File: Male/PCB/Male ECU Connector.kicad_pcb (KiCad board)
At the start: 2 copper layers, 135 x 41.5 mm, 34 parts, among them J1 ANALYZER, J2 ECU, J3 DJetECUEdgeConnector, U1 TLV76150DCYR, U2 DG333ADW-T1-E3, U3 DG333ADW-T1-E3, U4 DG419BDQ-T1-E3

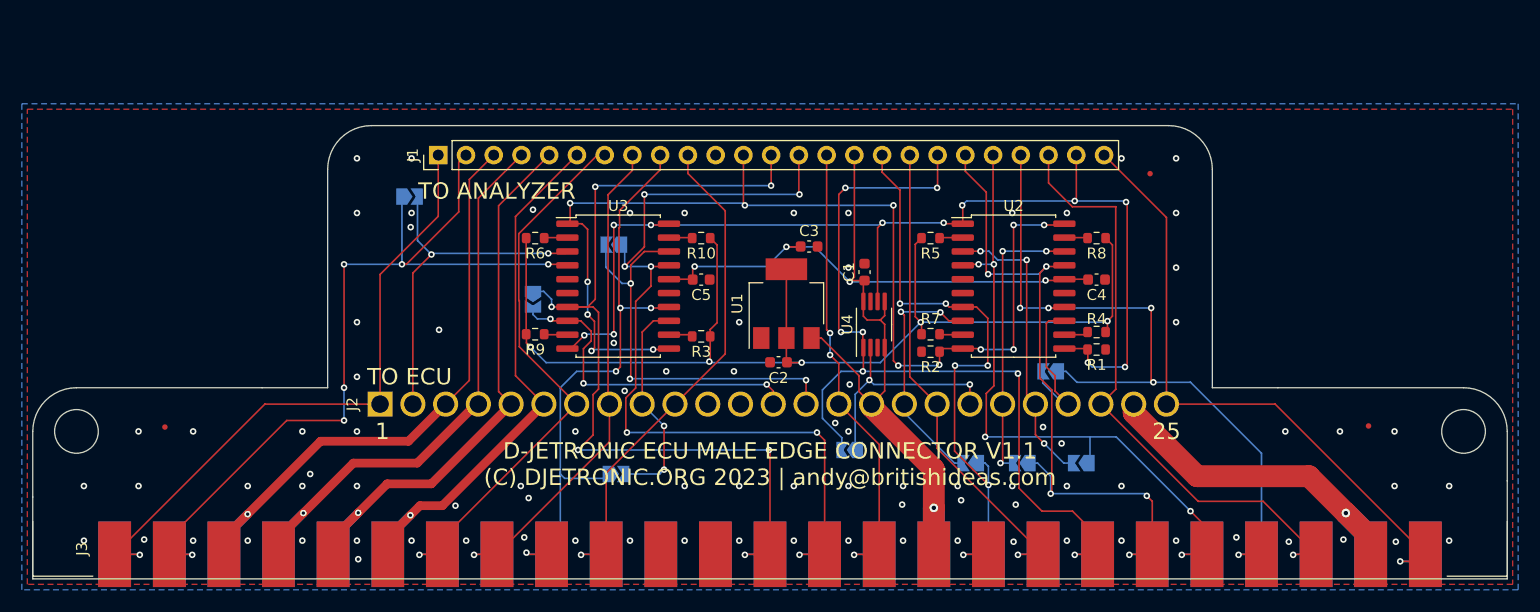
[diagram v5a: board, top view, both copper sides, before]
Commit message: Changed analyzer connector to DB25.
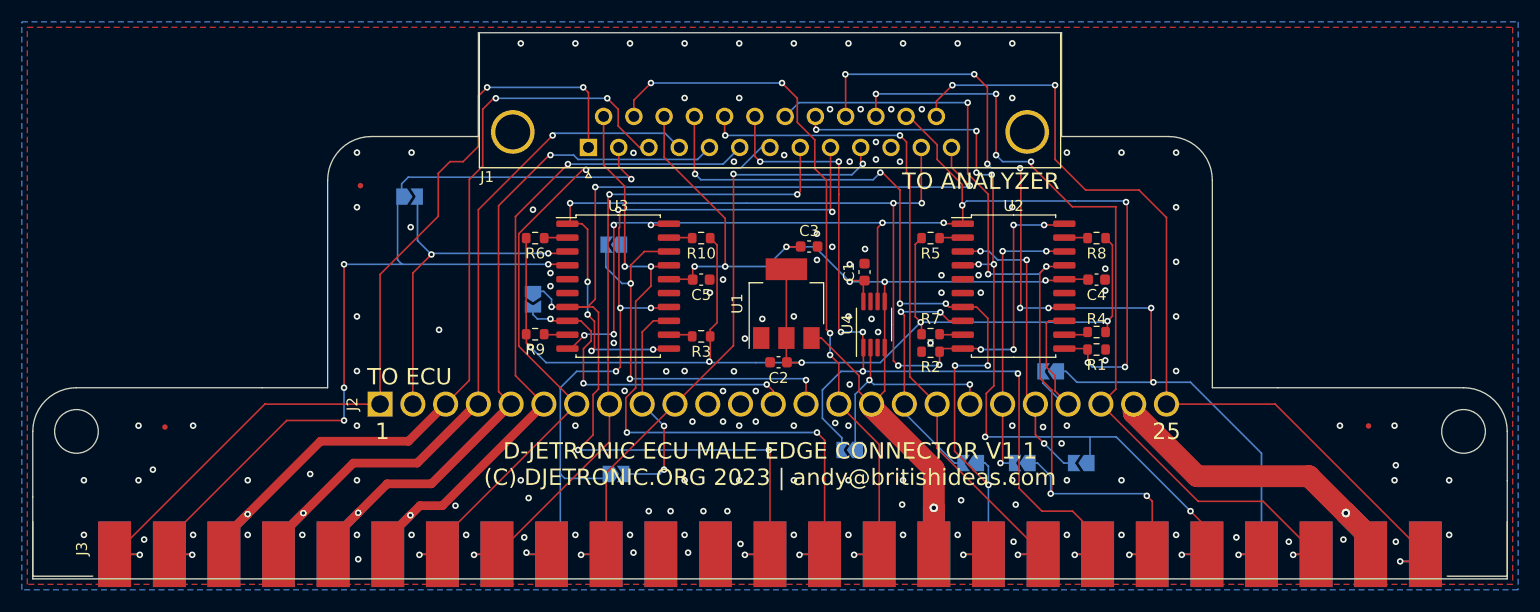
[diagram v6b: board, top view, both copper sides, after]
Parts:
- J1: footprint Connector_PinHeader_2.54mm:PinHeader_1x25_P2.54mm_Vertical -> Connector_Dsub:DSUB-25_Female_Horizontal_P2.77x2.84mm_EdgePinOffset7.70mm_Housed_MountingHolesOffset9.12mm
- moved FID3 72.3 mm to (112.0, 74.0)
- moved J1 13.8 mm to (132.9, 70.5), turned to 180 degrees
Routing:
- net /PGIII: track 69.6 -> 95.9 mm, vias 5 -> 9
- net Net-(J1-Pad15): track 43.2 -> 67.2 mm, vias 3 -> 5
- net Net-(J1-Pad25): track 59.7 -> 83.7 mm, vias 1 -> 3
- net Net-(J1-Pad1): track 59.6 -> 82.9 mm, vias 1 -> 3
- net /INJI: track 56.1 -> 78.3 mm, vias 1 -> 3
- net Net-(J1-Pad23): track 57.9 -> 80.1 mm, vias 1 -> 5
- net /TPS_ACCEL2: track 63.3 -> 85.2 mm, vias 5 -> 6
- net /TPS_IDLE: track 56.1 -> 77.5 mm, vias 6 -> 8
- net Net-(J1-Pad18): track 46.2 -> 66.2 mm, vias 1 -> 3
- net /PGII: track 84.4 -> 104.0 mm
- net /PGI: track 62.3 -> 81.9 mm, vias 5 -> 9
- net /TPS_ACCEL1: track 57.0 -> 76.2 mm, vias 4 -> 6
- net Net-(J1-Pad8): track 46.0 -> 63.2 mm, vias 1 -> 3
- net Net-(J1-Pad7): track 51.7 -> 67.2 mm, vias 1 -> 2
- net /INJII: track 52.8 -> 68.1 mm, vias 1 -> 2
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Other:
- board size 135 x 41.5 mm -> 135 x 50 mm
- board text added: "SOLDER ALL JUMPERS IF TOP COMPONENTS ARE NOT POPULATED"
- board text removed: "SOLDER ALL JUMPERS IF NO ANALYZER AND TOP COMPONENTS ARE NOT POPULATED"

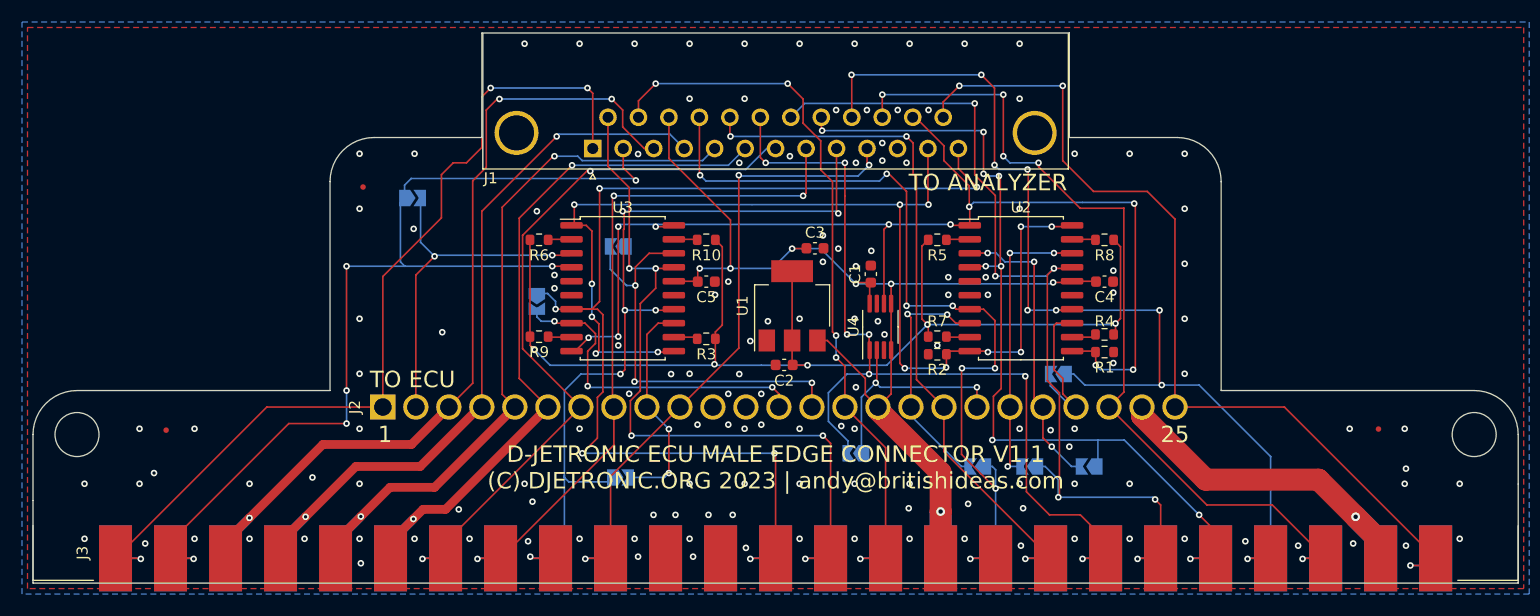
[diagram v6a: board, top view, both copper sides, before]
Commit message: Added additional mounting holes and reduced PCB size. Added first version of housing.
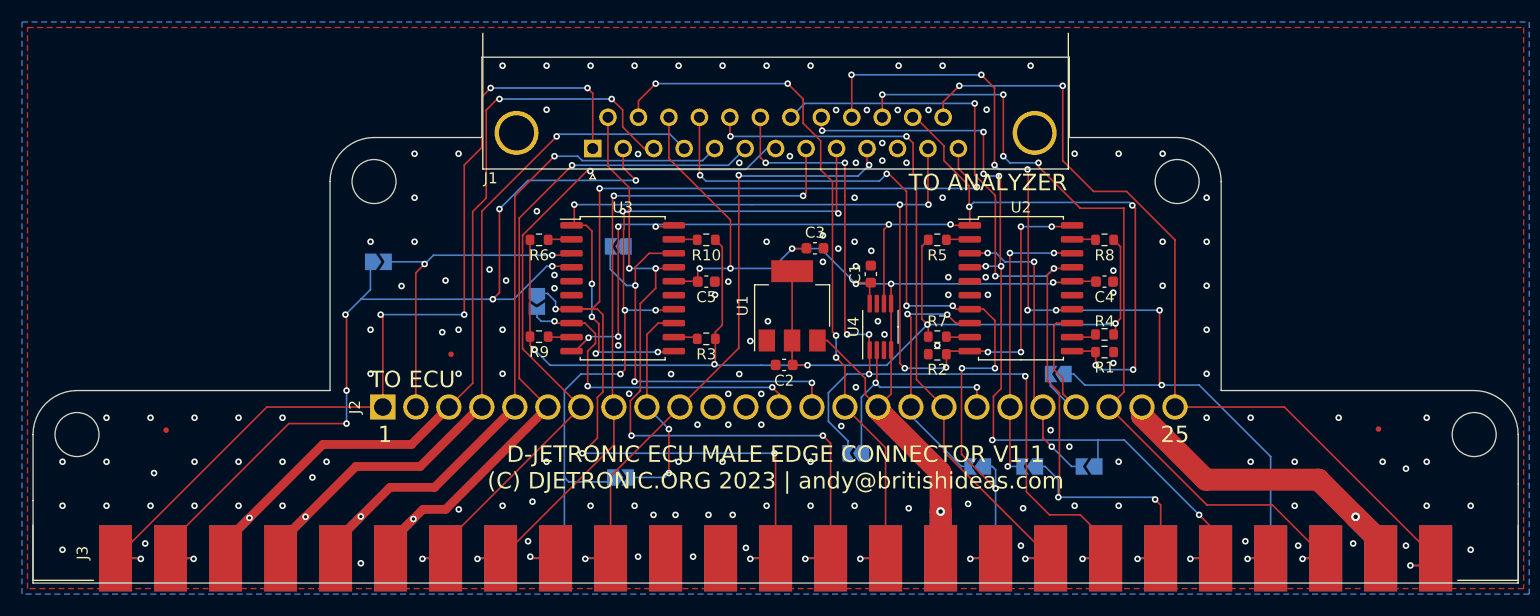
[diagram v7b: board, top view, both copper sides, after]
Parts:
- moved FID3 17.2 mm to (120.0, 89.2)
- moved JP4 6.58 mm to (113.4, 80.8)
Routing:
- net /TPS_WOT_DIAG_II_IV: track 93.4 -> 87.6 mm, vias 6 -> 8
- net Net-(J1-Pad1): track 82.9 -> 86.8 mm, vias 3 -> 5
- net /ECU_TPS_WOT_DIAG_II_IV: track 32.8 -> 30.6 mm
- net Net-(J1-Pad25): track 83.7 -> 82.6 mm
- net /INJII: track 68.1 -> 67.1 mm
- net /GND: vias 144 -> 155
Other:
- board size 135 x 50 mm -> 135 x 47.8 mm
